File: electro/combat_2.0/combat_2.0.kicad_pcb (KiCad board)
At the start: 2 copper layers, 65.8 x 50 mm, 26 parts, among them IC1 MCS1802GS-05-Z, J1 Screw_Terminal_01x02, J2 Screw_Terminal_01x02, J3 Screw_Terminal_01x02, J4 Screw_Terminal_01x02, Q1 AO4402G, Q2 AO4402G, Q3 AO4402G, Q4 AO4402G, U1 NodeMCU1.0(ESP-12E), U2 AZ1117CH-5.0TRG1, U3 TB6612FNG

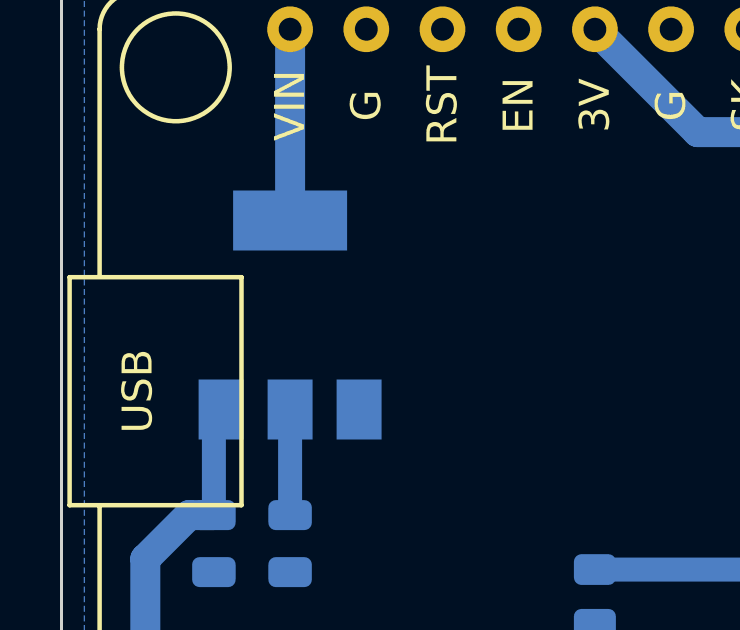
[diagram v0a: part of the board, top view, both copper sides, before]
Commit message: LDO connection fix
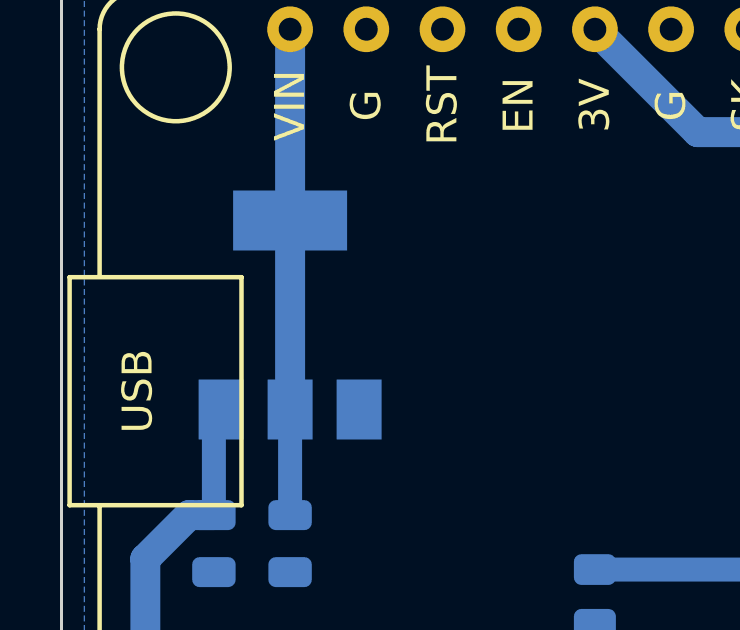
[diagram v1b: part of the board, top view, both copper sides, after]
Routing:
- net +5V: track 9.89 -> 16.2 mm
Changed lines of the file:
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@@
   (segment (start 89.845 113.24) (end 89.845 111.577) (width 0.4) (layer "B.Cu") (net 2))
   (segment (start 68.58 81.915) (end 68.58 88.29) (width 1) (layer "B.Cu") (net 3))
+  (segment (start 68.58 94.59) (end 68.58 88.29) (width 1) (layer "B.Cu") (net 3))
   (segment (start 68.58 98.11) (end 68.58 94.59) (width 0.8) (layer "B.Cu") (net 3))
   (segment (start 105.105 121.92) (end 105.105 120.345) (width 1) (layer "B.Cu") (net 4))

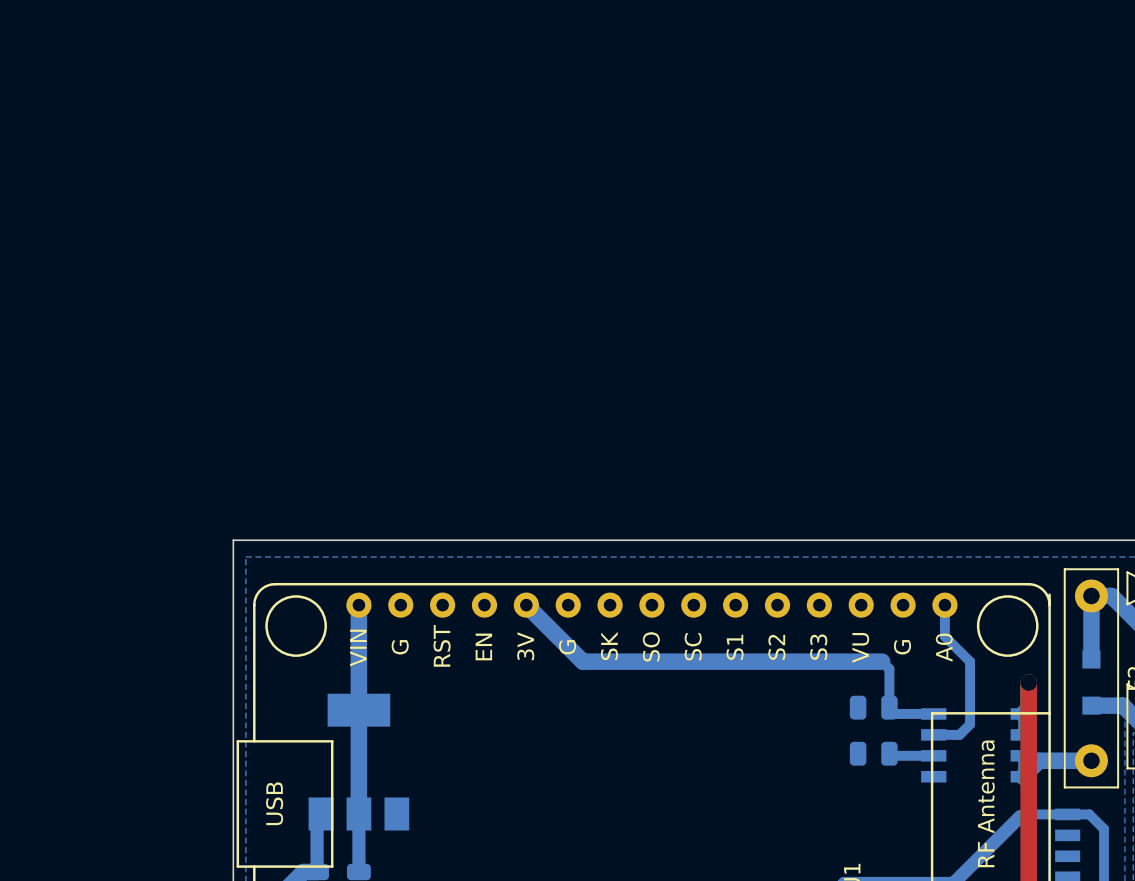
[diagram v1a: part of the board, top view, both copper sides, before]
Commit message: Changed resistors to SMD1206 type, hand-soldered version (slightly bigger pads)
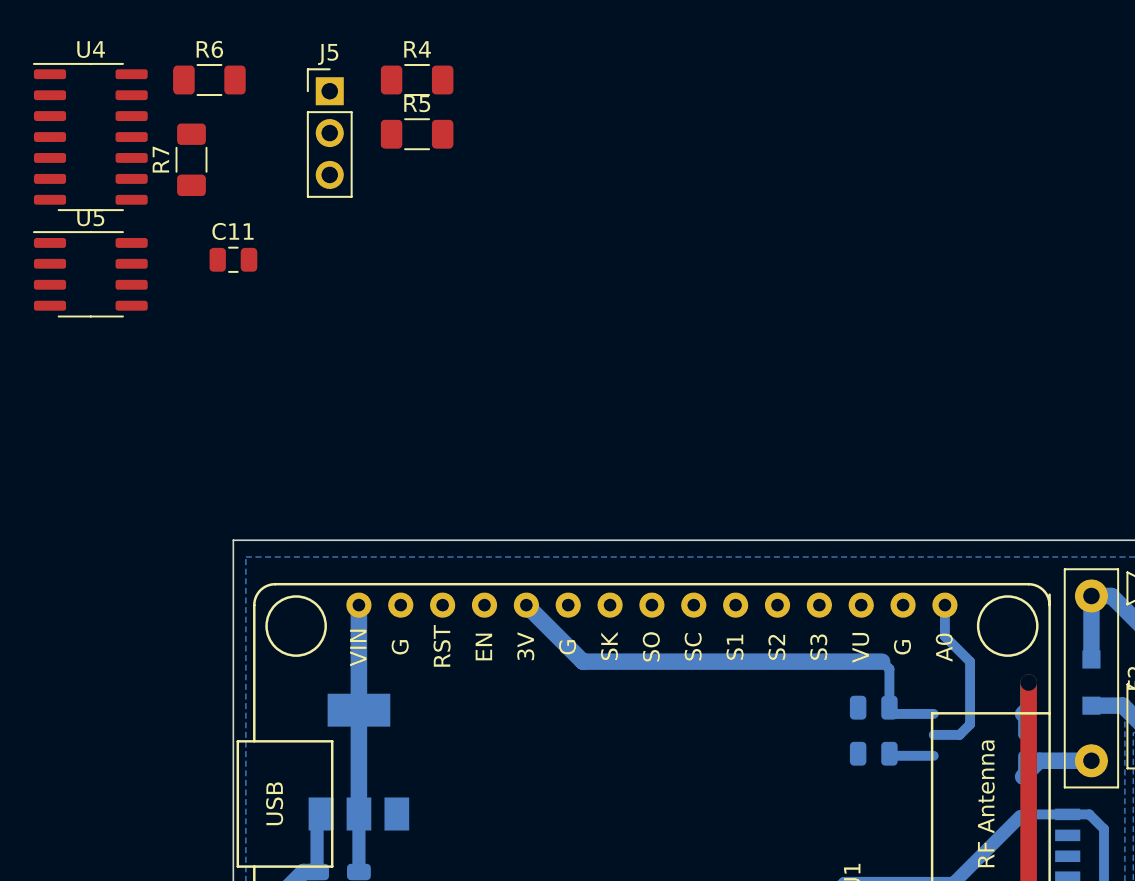
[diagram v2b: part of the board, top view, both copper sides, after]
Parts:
- removed IC1: MCS1802GS-05-Z, MCS1802GS:SOIC127P600X175-8N
- added C11: ~, Capacitor_SMD:C_0805_2012Metric, F.Cu at (61.0, 61.0)
- added J5: Conn_01x03_Pin, Connector_PinHeader_2.54mm:PinHeader_1x03_P2.54mm_Vertical, F.Cu at (66.8, 50.7)
- added R4: 8k2R, Resistor_SMD:R_1206_3216Metric_Pad1.30x1.75mm_HandSolder, F.Cu at (72.1, 50.0)
- added R5: 4k7R, Resistor_SMD:R_1206_3216Metric_Pad1.30x1.75mm_HandSolder, F.Cu at (72.1, 53.3)
- added R6: 2k7R, Resistor_SMD:R_1206_3216Metric_Pad1.30x1.75mm_HandSolder, F.Cu at (59.5, 50.0)
- added R7: 4k7R, Resistor_SMD:R_1206_3216Metric_Pad1.30x1.75mm_HandSolder, F.Cu at (58.4, 54.9)
- added U4: LM2902, Package_SO:SOIC-14_3.9x8.7mm_P1.27mm, F.Cu at (52.3, 53.5)
- added U5: ACS712xLCTR-20A, Package_SO:SOIC-8_3.9x4.9mm_P1.27mm, F.Cu at (52.3, 61.8)
- C10: value 1uF -> 0.1uF
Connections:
- net IN_B_1 renamed /DIR_B_1
- net IN_B_2 renamed /DIR_B_2
- net PWM_A renamed /PWM_CH_A
- net PWM_B renamed /PWM_CH_B
- net PWM_WEAPON renamed /PWM_WEAPON
- C10 pad 1: +3V3 -> +5V
- U1 pad 1: MOTOR_CURRENT_ADC -> /MOTOR_CURRENT_ADC
- U1 pad 18: unconnected-(U1-Pad18) -> /UART_TX
- U1 pad 19: unconnected-(U1-Pad19) -> /UART_RX
- U1 pad 27: IN__A_1 -> /DIR_A_1
- U1 pad 28: IN__A_2 -> /DIR_A_1
- U1 pad 3: unconnected-(U1-Pad3) -> /BAT_LVL_ADC
- U3 pad 21: IN__A_1 -> /DIR_A_1
- U3 pad 22: IN__A_2 -> /DIR_A_2
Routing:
- net IN__A_2: track 11.9 -> 0.00 mm
- net (no net): track 0.00 -> 11.9 mm
- net MOTOR_CURRENT_ADC: track 10.3 -> 0.00 mm
- net /MOTOR_CURRENT_ADC: track 0.00 -> 10.3 mm
- net IN__A_1: track 9.91 -> 0.00 mm
- net /DIR_A_1: track 0.00 -> 9.91 mm

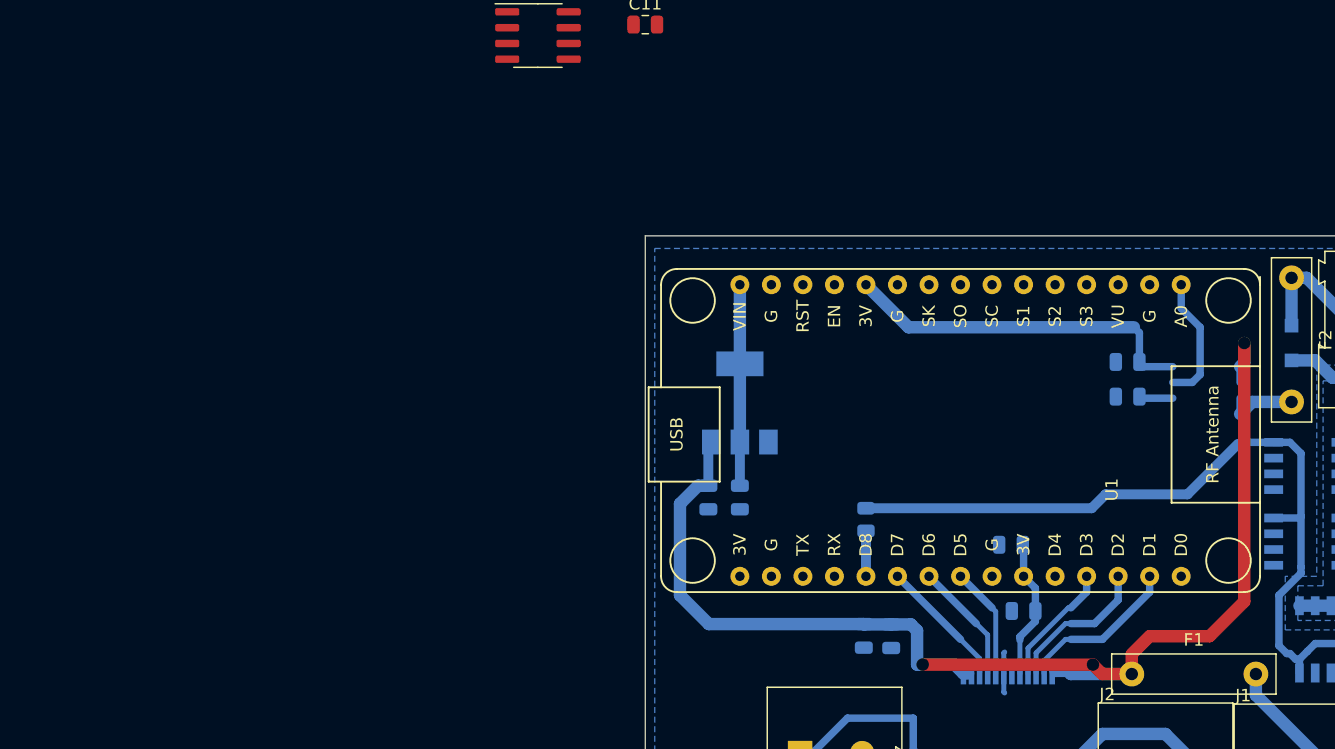
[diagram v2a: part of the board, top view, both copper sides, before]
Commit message: Changed MCU to ESP32-DEVKITC, cleared some ERC errors
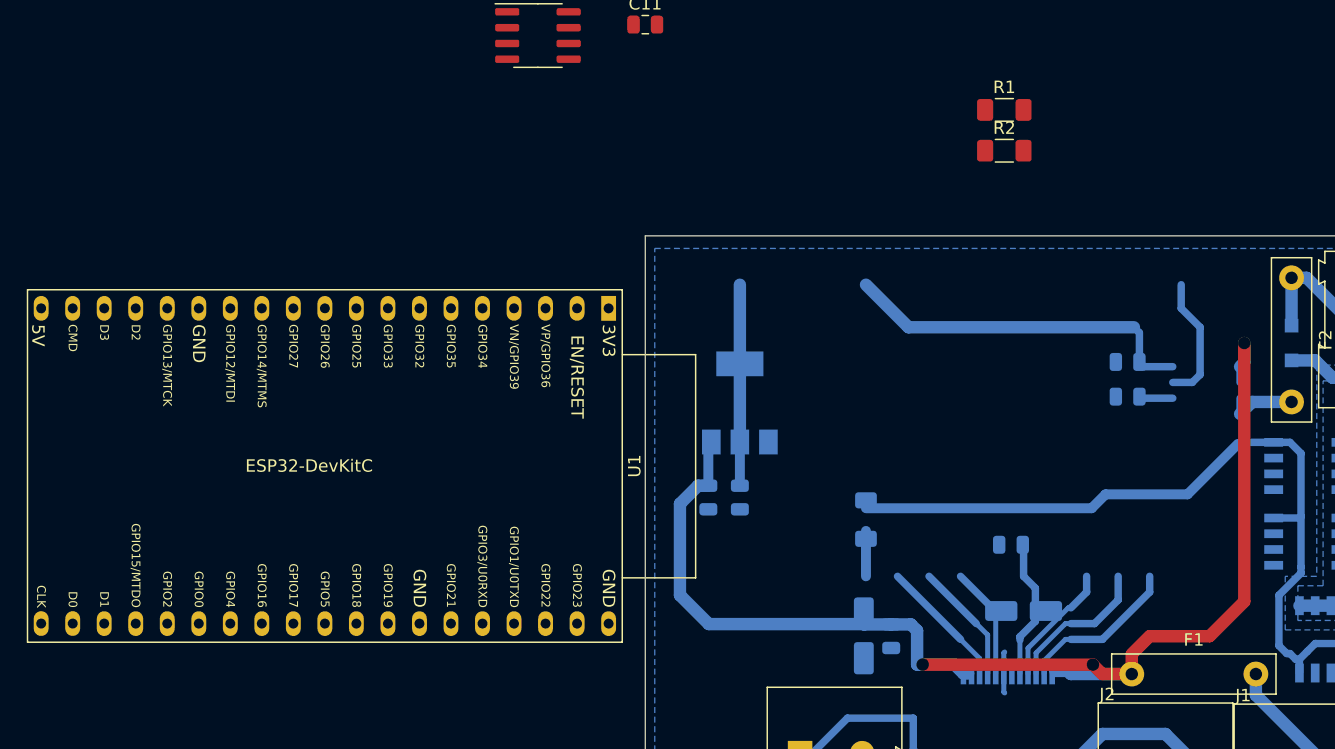
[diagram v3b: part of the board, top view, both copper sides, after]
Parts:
- added R1: 10k, Resistor_SMD:R_1206_3216Metric_Pad1.30x1.75mm_HandSolder, F.Cu at (89.9, 67.8)
- added R2: 10k, Resistor_SMD:R_1206_3216Metric_Pad1.30x1.75mm_HandSolder, F.Cu at (89.9, 71.1)
- C4, C8: footprint Capacitor_SMD:C_0805_2012Metric -> Capacitor_SMD:CP_Elec_4x5.4
- R3: footprint Resistor_SMD:R_0805_2012Metric -> Resistor_SMD:R_1206_3216Metric_Pad1.30x1.75mm_HandSolder
- U1: value NodeMCU1.0(ESP-12E) -> ESP32-DevKitC; footprint ESP8266:ESP12F-Devkit-V3 -> Espressif:ESP32-DevKitC
- moved U1 28.9 mm to (58.0, 83.8)
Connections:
- U1 pad 1: /MOTOR_CURRENT_ADC -> +3V3
- U1 pad 10: GND -> unconnected-(U1-DAC_2/ADC2_CH9/GPIO26-Pad10)
- U1 pad 11: +3V3 -> unconnected-(U1-ADC2_CH7/GPIO27-Pad11)
- U1 pad 15: +5V -> unconnected-(U1-MTCK/GPIO13/ADC2_CH4-Pad15)
- U1 pad 17: GND -> unconnected-(U1-SD_DATA3/GPIO10-Pad17)
- U1 pad 18: /UART_TX -> unconnected-(U1-CMD-Pad18)
- U1 pad 19: /UART_RX -> +5V
- U1 pad 20: /PWM_WEAPON -> unconnected-(U1-SD_CLK/GPIO6-Pad20)
- U1 pad 21: /PWM_CH_B -> unconnected-(U1-SD_DATA0/GPIO7-Pad21)
- U1 pad 22: /DIR_B_2 -> unconnected-(U1-SD_DATA1/GPIO8-Pad22)
- U1 pad 23: /DIR_B_1 -> unconnected-(U1-MTDO/GPIO15/ADC2_CH3-Pad23)
- U1 pad 24: GND -> /MOTOR_CURRENT_ADC
- U1 pad 25: +3V3 -> unconnected-(U1-GPIO0/BOOT/ADC2_CH1-Pad25)
- U1 pad 26: unconnected-(U1-D4(GPIO2)-Pad26) -> /PWM_CH_A
- U1 pad 27: /DIR_A_1 -> unconnected-(U1-GPIO16-Pad27)
- U1 pad 28: /DIR_A_1 -> unconnected-(U1-GPIO17-Pad28)
- U1 pad 29: /PWM_CH_A -> /PWM_CH_B
- U1 pad 3: /BAT_LVL_ADC -> unconnected-(U1-SENSOR_VP/GPIO36/ADC1_CH0-Pad3)
- U1 pad 30: unconnected-(U1-D0(GPIO16)-Pad30) -> /DIR_A_1
- U1 pad 9: unconnected-(U1-CLK(SCLK)-Pad9) -> /BAT_LVL_ADC
- U4 pad 1: (no net) -> /PWM_WEAPON
- U4 pad 2: (no net) -> /weapon_motor/1.65V
- U4 pad 3: (no net) -> /PWM_WEAPON
- U4 pad 5: /PWM_WEAPON -> (no net)
- U4 pad 6: /weapon_motor/1.65V -> (no net)
- U4 pad 7: /PWM_WEAPON -> (no net)
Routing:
- net +5V: track 16.2 -> 45.0 mm
- net +3V3: track 40.1 -> 11.3 mm
- net /DIR_A_2: track 0.00 -> 11.9 mm
- net (no net): track 11.9 -> 0.00 mm

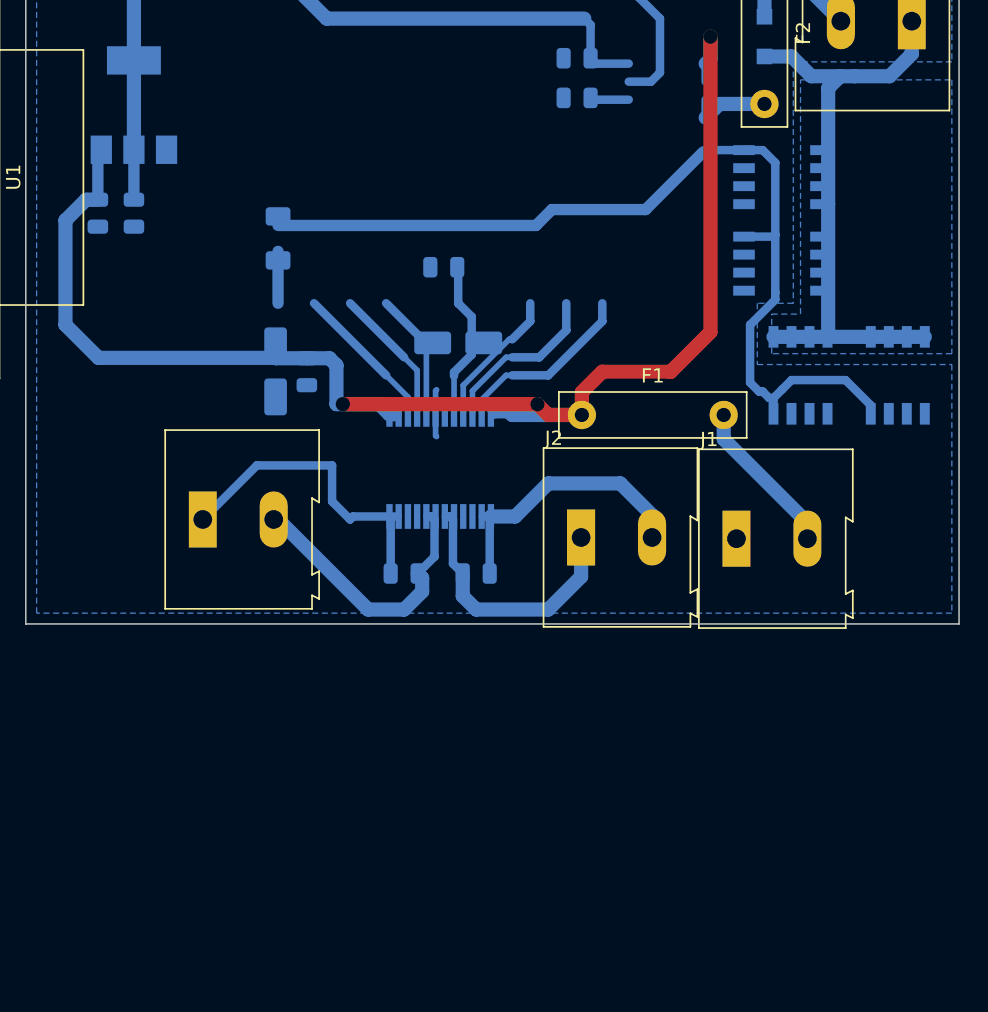
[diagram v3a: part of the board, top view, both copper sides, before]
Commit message: Updated some footprints
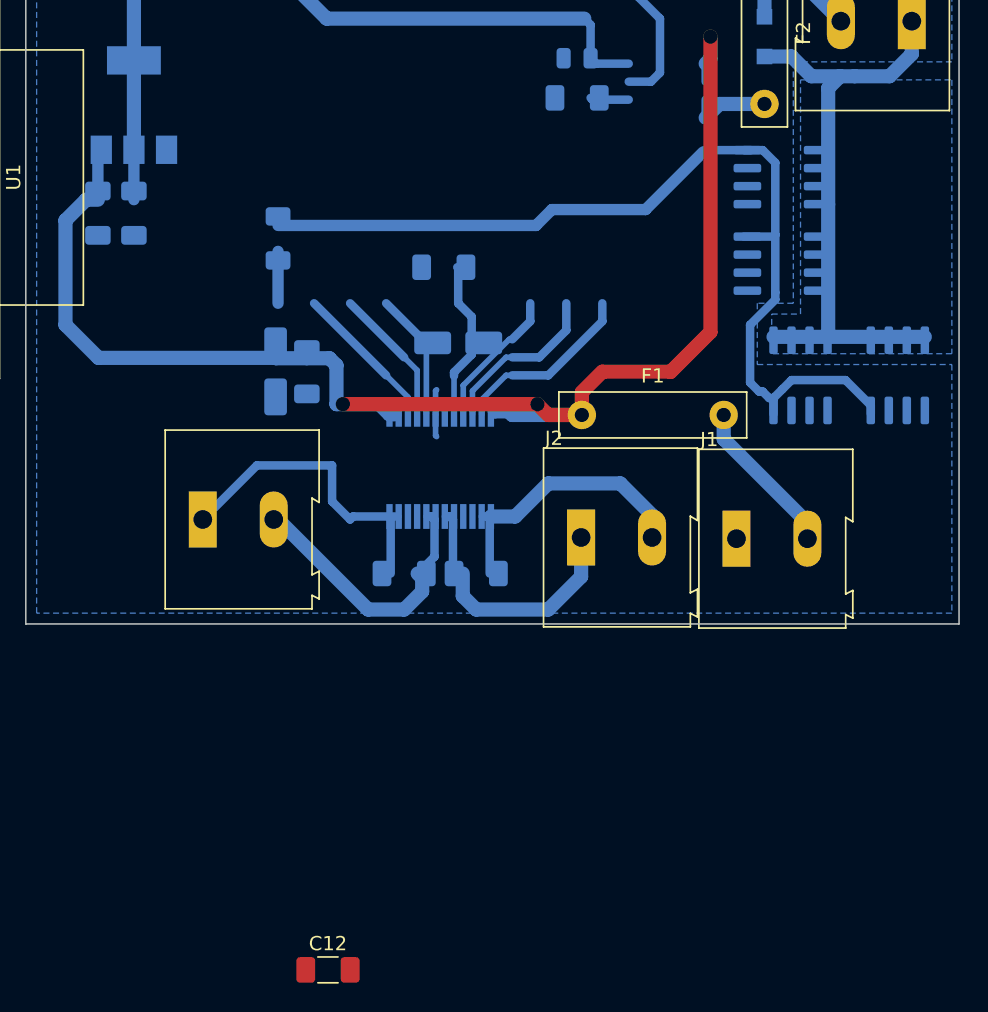
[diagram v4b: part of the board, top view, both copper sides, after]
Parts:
- added C12: 0.1uF, Capacitor_SMD:C_1206_3216Metric_Pad1.33x1.80mm_HandSolder, F.Cu at (82.3, 152.4)
- C1, C2, C3, C5, C6, C7, C9: footprint Capacitor_SMD:C_0805_2012Metric -> Capacitor_SMD:C_1206_3216Metric_Pad1.33x1.80mm_HandSolder
- Q1, Q2, Q3, Q4: footprint MCS1802GS:SOIC127P600X175-8N -> Package_SO:SOIC-8_3.9x4.9mm_P1.27mm
